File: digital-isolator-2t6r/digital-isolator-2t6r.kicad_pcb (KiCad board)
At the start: 2 copper layers, 47.1 x 42 mm, 34 parts, among them J1 Conn_02x08_Odd_Even, J2 Conn_02x08_Odd_Even, U1 ADuM1401xRW, U2 ADuM1401xRW

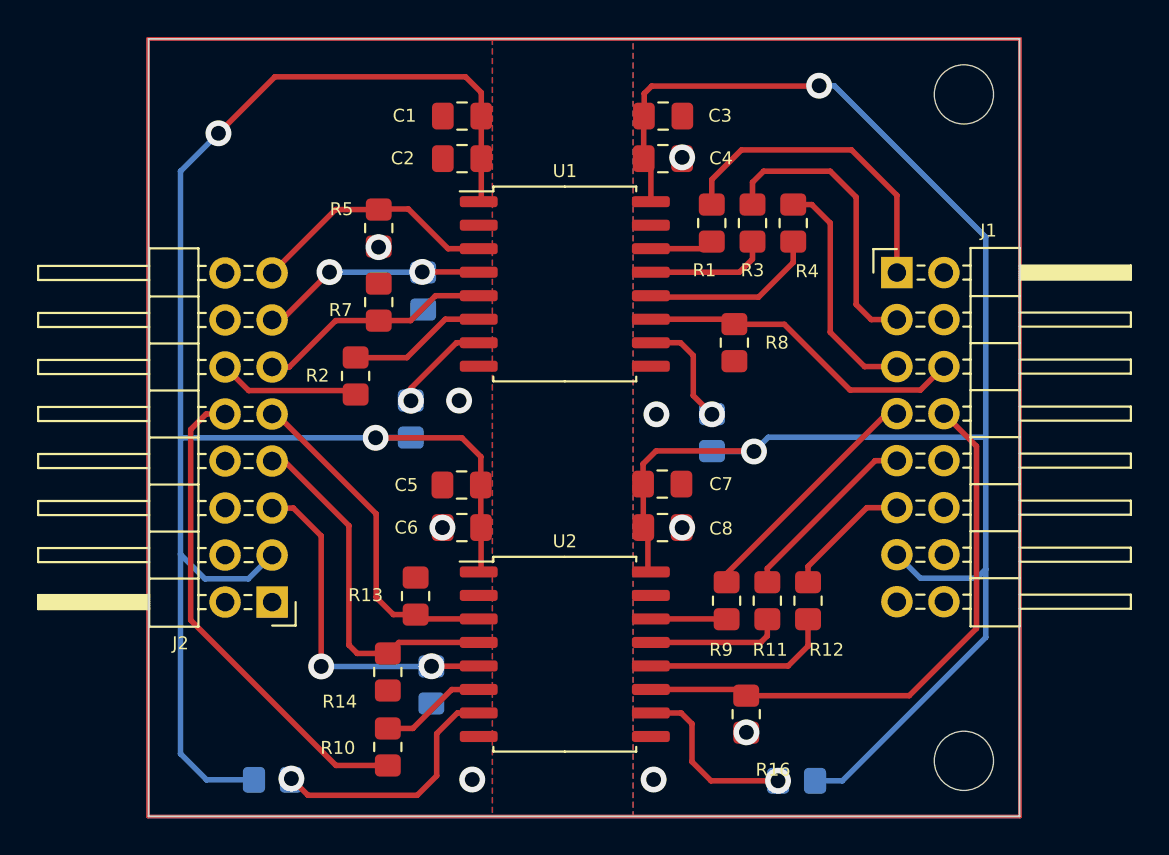
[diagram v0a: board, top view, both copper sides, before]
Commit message: Adapted dig iso 6t2r for jlcpcb
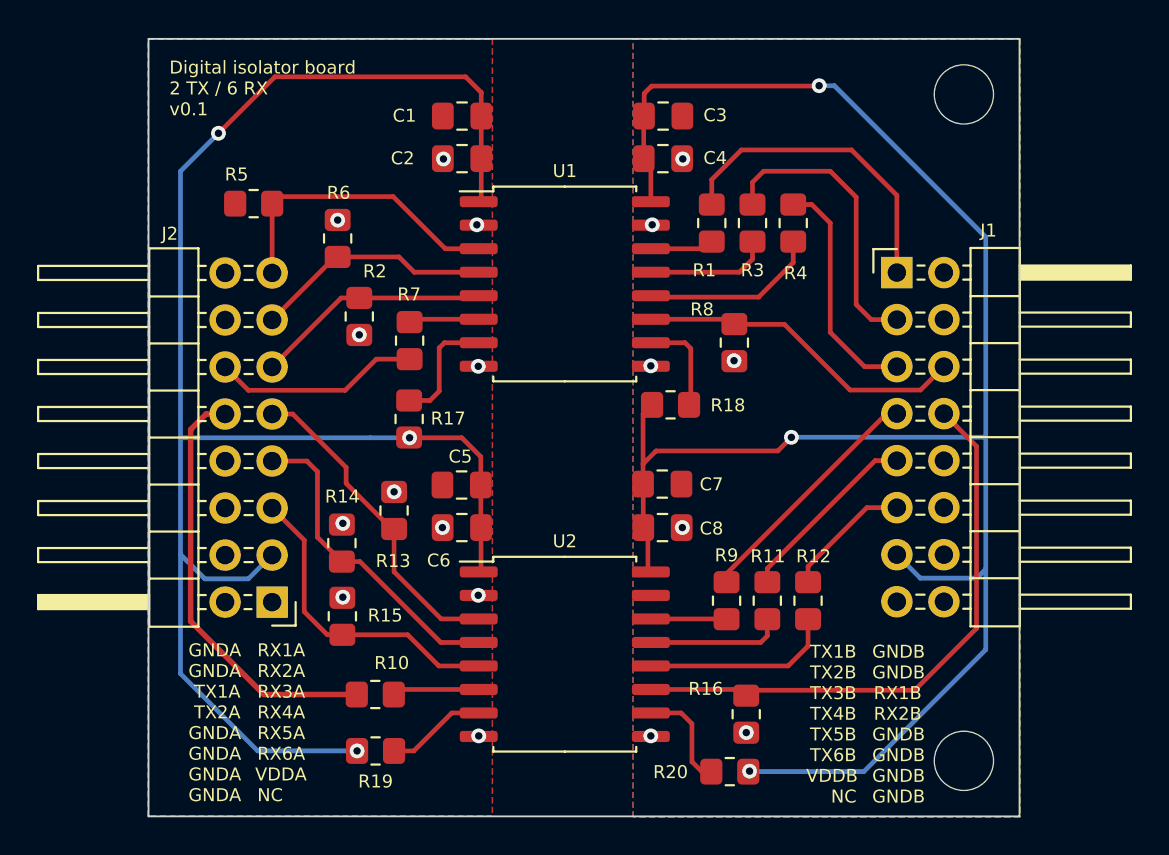
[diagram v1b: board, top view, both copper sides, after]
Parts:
- R15, R17, R18, R19, R20, R6: moved to F.Cu
- moved R14 7.39 mm to (102.8, 50.1), turned to 90 degrees
- moved R5 6.88 mm to (98.1, 31.8), turned to 180 degrees
- moved R15 6.07 mm to (102.8, 54.0), turned to 90 degrees
- moved R19 5.78 mm to (104.6, 61.3)
- moved R6 5.42 mm to (102.6, 33.6), turned to 90 degrees
- moved R13 4.77 mm to (105.6, 48.3)
- moved R20 3.64 mm to (123.8, 62.4)
- moved R2 3.49 mm to (106.5, 39.2)
- moved R10 2.91 mm to (104.6, 58.3), turned to 180 degrees
- moved R18 2.69 mm to (120.6, 42.6), turned to 0 degrees
- moved R7 1.31 mm to (103.8, 37.8), turned to -90 degrees
- moved R17 0.09 mm to (106.5, 43.4)
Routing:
- net Net-(R19-Pad1): track 13.7 -> 5.42 mm, vias 1 -> 0
- net VDDB: track 95.0 -> 99.9 mm, vias 2 -> 3
- net Net-(R20-Pad2): track 9.59 -> 5.78 mm, vias 1 -> 0
- net /adum241x/TX1_A': track 7.51 -> 3.80 mm
- net /TX1_A: track 7.67 -> 11.2 mm
- net /TX2_A: track 26.4 -> 23.2 mm
- net /RX1_A: track 13.5 -> 16.2 mm
- net /RX5_A: track 19.5 -> 17.3 mm
- net /RX6_A: track 18.8 -> 17.0 mm, vias 2 -> 0
- net /RX4_A: track 18.9 -> 17.6 mm
- net /adum241x1/TX1_A': track 5.78 -> 4.70 mm
- net Net-(R17-Pad1): track 5.36 -> 6.42 mm, vias 1 -> 0
- net Net-(R18-Pad2): track 6.17 -> 5.37 mm, vias 1 -> 0
- net VDDA: track 92.8 -> 92.0 mm, vias 2 -> 3
- net /RX2_A: track 12.2 -> 12.9 mm, vias 2 -> 0
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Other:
- board text added: "Digital isolator board 2 TX / 6 RX v0.1"
- board text added: "GNDA"
- board text added: "GNDB"
- board text added: "NC"
- board text added: "RX1A"
- board text added: "RX1B"
- board text added: "RX2A"
- board text added: "RX2B"
- board text added: "RX3A"
- board text added: "RX4A"
- board text added: "RX5A"
- board text added: "RX6A"
- board text added: "TX1A"
- board text added: "TX1B"
- board text added: "TX2A"
- board text added: "TX2B"
- board text added: "TX3B"
- board text added: "TX4B"
- board text added: "TX5B"
- board text added: "TX6B"
- board text added: "VDDA"
- board text added: "VDDB"
